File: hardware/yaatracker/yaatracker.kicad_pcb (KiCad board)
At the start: 2 copper layers, 62 parts, among them J1 USB_MINI, P1 TP_URX, P10 BATT, P11 MBUTTON2, P12 ICSP_CONN5, P13 I2C_SCREEN, P14 R_VCC, P15 GPS_DE9, P16 RADIO_DE9, P2 GPIO10_GND_JUMPER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

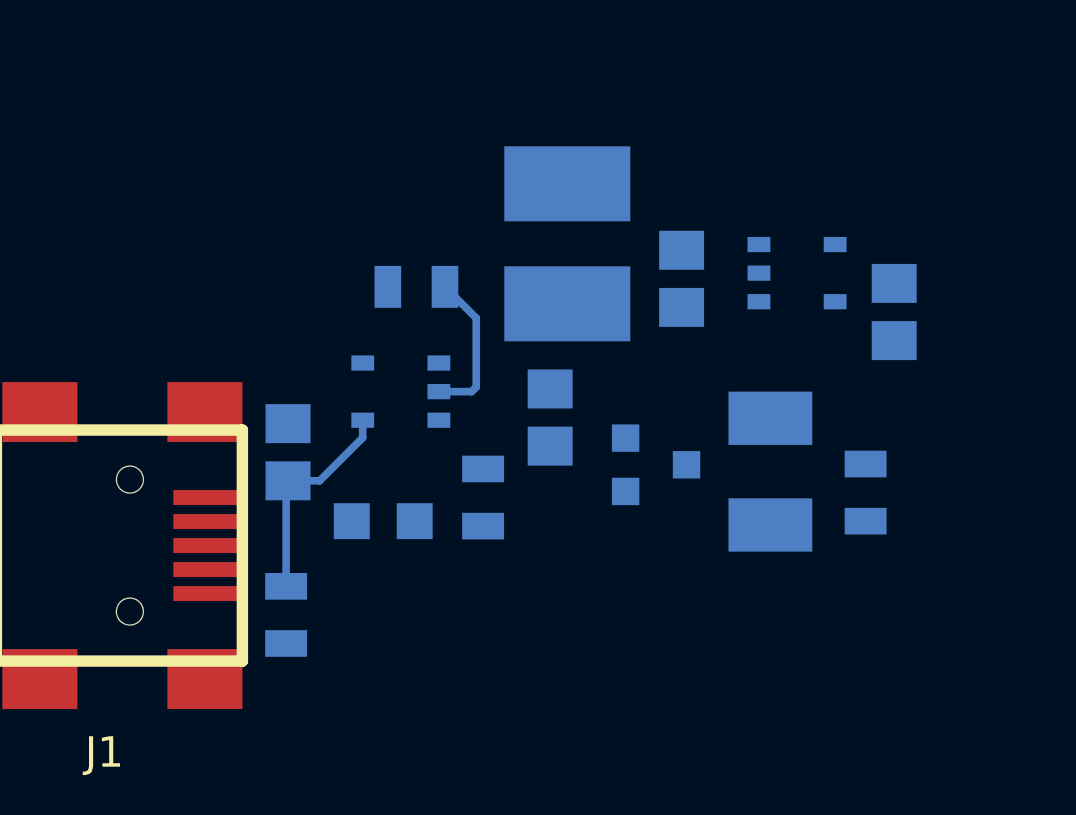
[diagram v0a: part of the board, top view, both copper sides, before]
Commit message: PCB layout power circuit finished
Layout of the power circuit is now finished
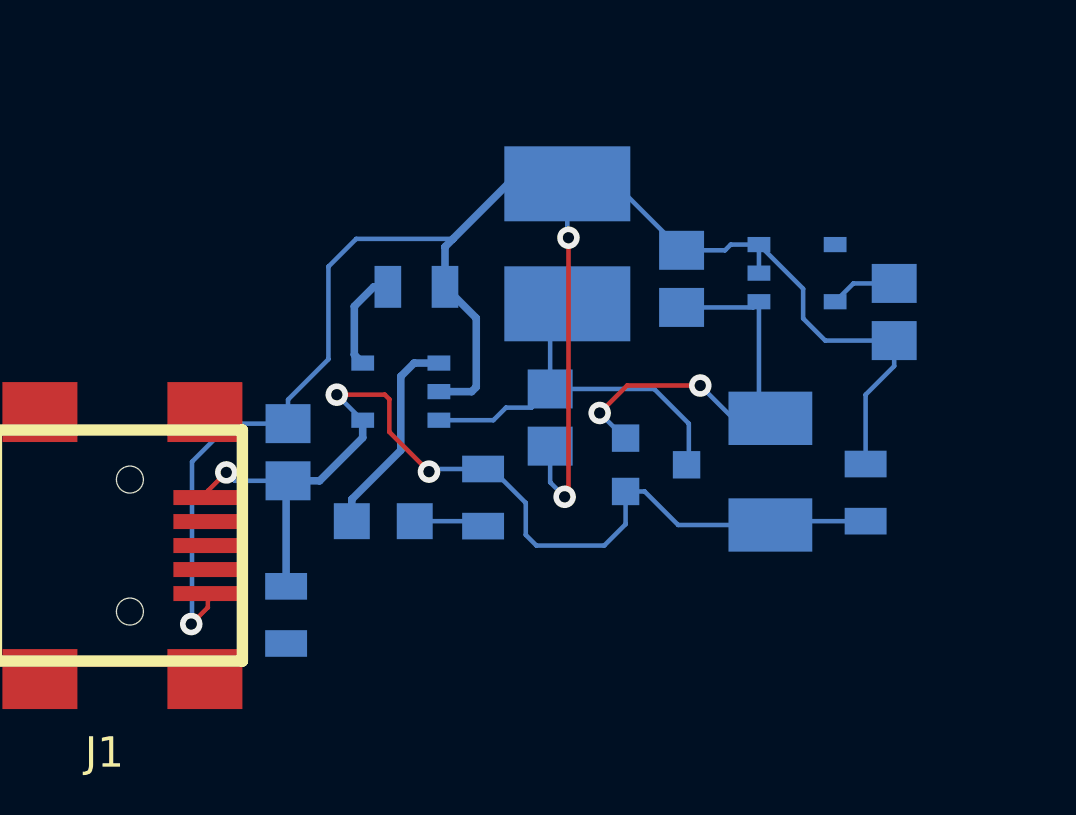
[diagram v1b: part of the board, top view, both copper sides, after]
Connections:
- R18 pad 1: N-0000026 (its old number) -> GND
- U4 pad 2: N-0000026 (its old number) -> GND
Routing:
- net GND: track 0.00 -> 63.7 mm, vias 0 -> 3
- net N-0000035: track 7.21 -> 34.6 mm, vias 0 -> 3
- net N-0000025: track 0.00 -> 14.4 mm, vias 0 -> 2
- net N-0000027: track 0.00 -> 13.7 mm
- net N-0000036: track 0.00 -> 6.96 mm
- net N-0000026 (its old number): track 5.08 -> 0.00 mm
- net N-0000024: track 0.00 -> 3.39 mm
- net N-0000037: track 0.00 -> 2.35 mm
- net +3.3V: track 0.00 -> 2.22 mm
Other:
- net class Default: clearance 0.254 -> 0.1524; trace_width 0.254 -> 0.1524; via_dia 0.889 -> 0.75; via_drill 0.635 -> 0.5
- net class power added: clearance 0.1524, trace_width 0.23, via_dia 0.75, via_drill 0.5
- rule trace_clearance: 0.254 -> 0.1524
- rule trace_min: 0.254 -> 0.1524
- rule via_min_drill: 0.508 -> 0.4
- rule via_min_size: 0.889 -> 0.75

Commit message: More PCB layout
ICSP connector done, as well as screen/I2C connector, and a few buttons.
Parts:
- moved P12 222.6 mm to (113.7, 120.4), turned to 180 degrees
- moved R17 220.5 mm to (122.5, 124.0)
- moved R14 216.5 mm to (123.9, 127.0), turned to 90 degrees
- moved R13 214.3 mm to (122.2, 131.1), turned to 90 degrees
- moved R15 195.0 mm to (136.6, 123.3)
- moved C10 192.1 mm to (113.7, 140.0), turned to 180 degrees
- moved P13 122.0 mm to (133.0, 120.0)
- moved R16 100.2 mm to (121.5, 127.3), turned to 270 degrees
- moved R12 88.3 mm to (130.5, 123.1), turned to 180 degrees
- moved U3 39.7 mm to (122.5, 139.4)
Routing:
- net N-000001: track 0.00 -> 49.9 mm
- net +3.3V: track 2.22 -> 39.1 mm, vias 0 -> 2
- net GND: track 63.7 -> 99.3 mm, vias 3 -> 4
- net N-0000020: track 0.00 -> 29.4 mm
- net N-0000021: track 0.00 -> 24.0 mm
- net N-0000044: track 0.00 -> 21.5 mm, vias 0 -> 2
- net N-0000043: track 0.00 -> 17.1 mm
- net N-0000019: track 0.00 -> 9.77 mm
- net N-000007: track 0.00 -> 6.93 mm
- net N-000008: track 0.00 -> 2.82 mm
- net N-0000011: track 0.00 -> 2.27 mm
- net N-000009: track 0.00 -> 2.24 mm
- net N-0000035: track 34.6 -> 33.3 mm

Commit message: Some more PCB layout
Some more PCB layout. Forgot to connect two grounds together.
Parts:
- C8: moved to B.Cu
- moved R5 205.8 mm to (140.8, 141.3), turned to 180 degrees
- moved R11 203.5 mm to (138.8, 138.4), turned to 270 degrees
- moved C4 188.0 mm to (141.7, 138.2), turned to 270 degrees
- moved C8 169.3 mm to (130.5, 138.0), turned to 90 degrees
- moved U2 133.5 mm to (133.5, 138.0)
- moved P15 102.1 mm to (142.4, 124.5), turned to 270 degrees
- moved P8 96.4 mm to (136.8, 132.0)
- moved R8 81.0 mm to (136.7, 141.1), turned to 180 degrees
- moved P16 58.2 mm to (209.8, 131.2), turned to 270 degrees
- moved RV2 55.8 mm to (162.4, 131.3)
- moved P4 49.7 mm to (157.3, 153.5)
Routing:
- net (no net): track 0.00 -> 28.8 mm
- net +3.3V: track 39.1 -> 64.5 mm, vias 2 -> 4
- net /UART_RX: track 0.00 -> 22.0 mm
- net N-0000038: track 0.00 -> 18.1 mm
- net N-000003: track 0.00 -> 7.39 mm, vias 0 -> 2
- net GND: track 99.3 -> 106.6 mm
- net N-0000042: track 0.00 -> 6.39 mm, vias 0 -> 1
- net N-000004: track 0.00 -> 6.36 mm
- net N-000005: track 0.00 -> 4.46 mm
- net N-000006: track 0.00 -> 2.15 mm

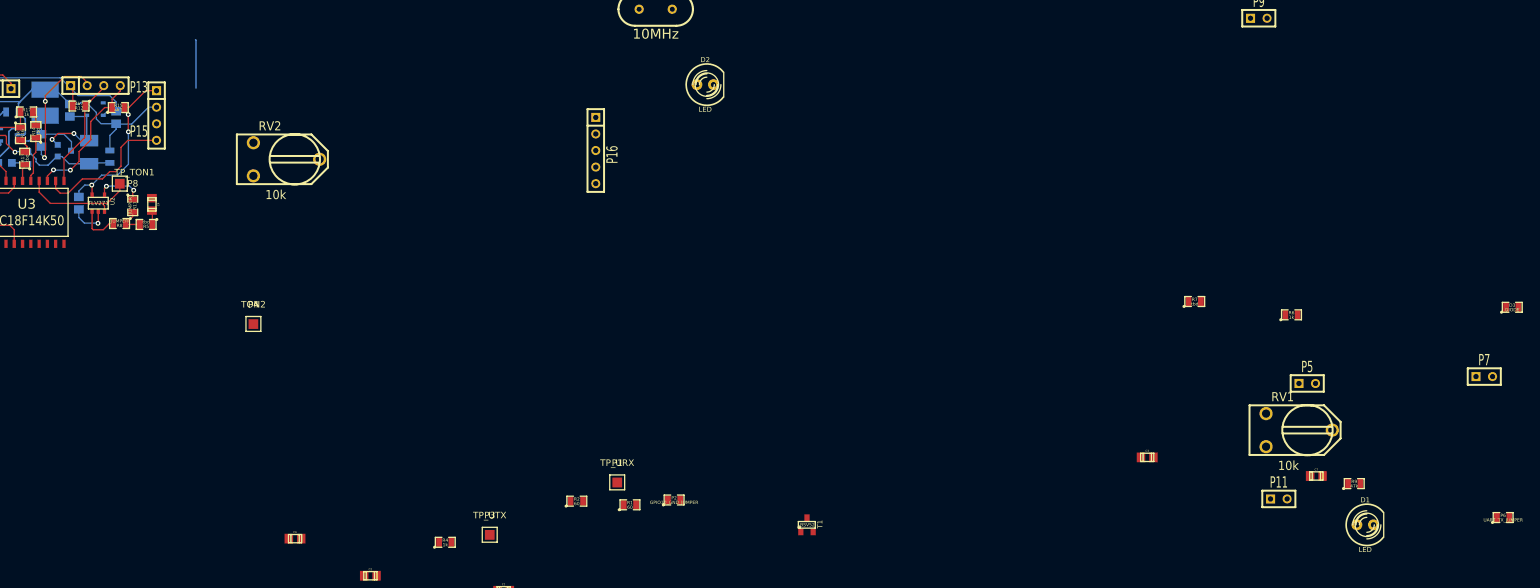
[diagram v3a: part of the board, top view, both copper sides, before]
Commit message: Traces to GPS conn, audio out
Routed traces to GPS uart connector, and audio out done to pot.
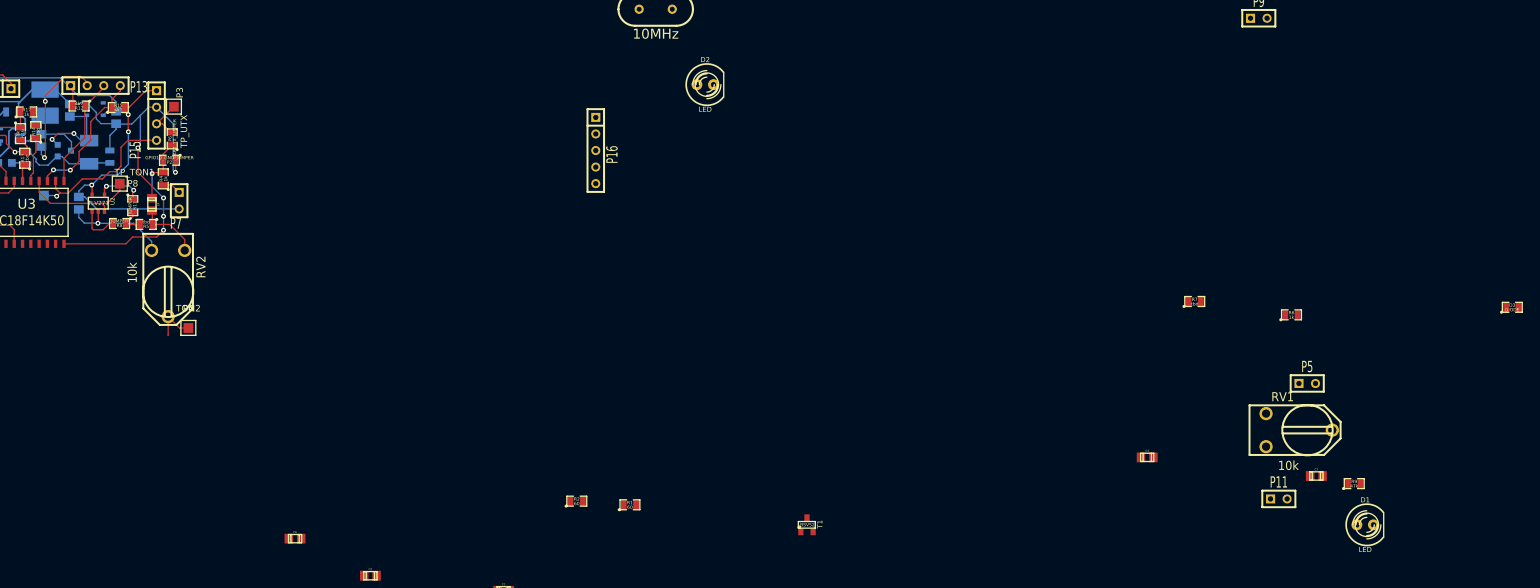
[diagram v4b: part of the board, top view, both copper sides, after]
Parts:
- P1: moved to B.Cu
- moved P6 212.3 mm to (144.8, 128.1), turned to 90 degrees
- moved P7 202.1 mm to (145.9, 137.6), turned to 270 degrees
- moved P1 95.8 mm to (125.1, 139.8)
- moved P2 93.3 mm to (144.4, 131.4), turned to 180 degrees
- moved P3 81.6 mm to (145.1, 120.2)
- moved R4 70.6 mm to (143.4, 134.3), turned to 90 degrees
- moved RV2 26.3 mm to (144.2, 150.3), turned to 270 degrees
- moved P4 10.0 mm to (147.3, 154.2)
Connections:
- C4 pad 2: N-0000042 -> GND
- C7 pad 2: N-0000042 -> GND
- C8 pad 2: N-0000042 -> GND
- R6 pad 1: N-0000042 -> GND
- RV2 pad 3: N-0000042 -> GND
- T1 pad 2: N-0000042 -> GND
- U2 pad 2: N-0000042 -> GND
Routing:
- net GND: track 106.6 -> 150.6 mm, vias 4 -> 7
- net N-0000018: track 0.00 -> 32.1 mm, vias 0 -> 4
- net +3.3V: track 64.5 -> 80.6 mm
- net N-000001: track 2.15 -> 9.75 mm
- net (no net): track 28.8 -> 21.3 mm
- net /UART_TX: track 0.00 -> 6.71 mm
- net /AUDIO_OUT: track 0.00 -> 6.68 mm
- net N-0000042: track 6.39 -> 0.00 mm, vias 1 -> 0
- net N-000007: track 0.00 -> 2.91 mm
- net /UART_RX: track 22.0 -> 24.7 mm, vias 0 -> 1

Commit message: PCB layout almost finished
Lacking LEDs, and a few buttons to be routed.
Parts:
- moved D3 231.9 mm to (120.0, 180.5)
- moved P11 210.2 mm to (108.4, 142.9)
- moved P5 208.4 mm to (110.8, 175.3)
- moved P9 203.1 mm to (111.9, 147.1)
- moved R9 201.7 mm to (126.1, 155.3), turned to 270 degrees
- moved C7 194.3 mm to (127.1, 159.2), turned to 180 degrees
- moved RV1 186.6 mm to (132.2, 153.7), turned to 270 degrees
- moved C3 157.6 mm to (137.9, 158.8), turned to 180 degrees
- moved R3 122.5 mm to (119.6, 176.7)
- moved T1 117.6 mm to (127.3, 162.3), turned to 270 degrees
- moved X1 110.9 mm to (116.9, 151.5), turned to 180 degrees
- moved C1 97.9 mm to (108.4, 153.2), turned to 180 degrees
- moved C2 80.3 mm to (108.4, 150.6), turned to 180 degrees
- moved P16 75.3 mm to (142.0, 164.1), turned to 0 degrees
- moved C6 68.1 mm to (113.9, 142.9), turned to 180 degrees
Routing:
- net GND: track 150.6 -> 223.5 mm, vias 7 -> 11
- net +3.3V: track 80.6 -> 131.7 mm, vias 4 -> 5
- net /R_VOUT: track 0.00 -> 47.7 mm, vias 0 -> 2
- net N-0000011: track 2.27 -> 39.7 mm, vias 0 -> 2
- net N-0000010: track 2.24 -> 36.3 mm, vias 0 -> 1
- net N-0000025: track 0.00 -> 21.5 mm
- net N-0000028: track 0.00 -> 18.2 mm
- net N-0000027: track 0.00 -> 14.2 mm
- net N-0000040: track 0.00 -> 10.3 mm
- net /PTT: track 0.00 -> 8.06 mm
- net /AUDIO_OUT: track 6.68 -> 13.9 mm
- net /AUDIO_IN: track 0.00 -> 5.48 mm
- net N-0000041: track 0.00 -> 5.13 mm
- net N-0000033: track 33.3 -> 32.4 mm

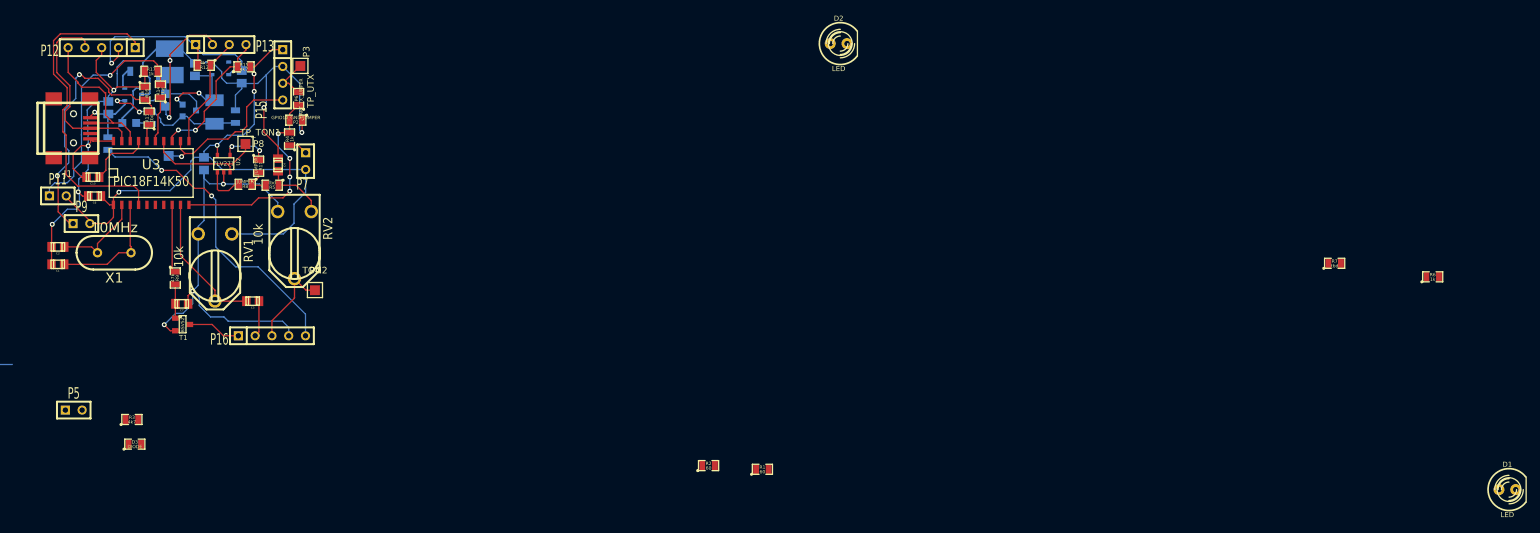
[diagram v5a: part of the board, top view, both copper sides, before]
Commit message: PCB layout routing done
PCB layout traces routing done, but need to add a button connected to pin 7 (pull down
and current-limiting resistor already exist in design).
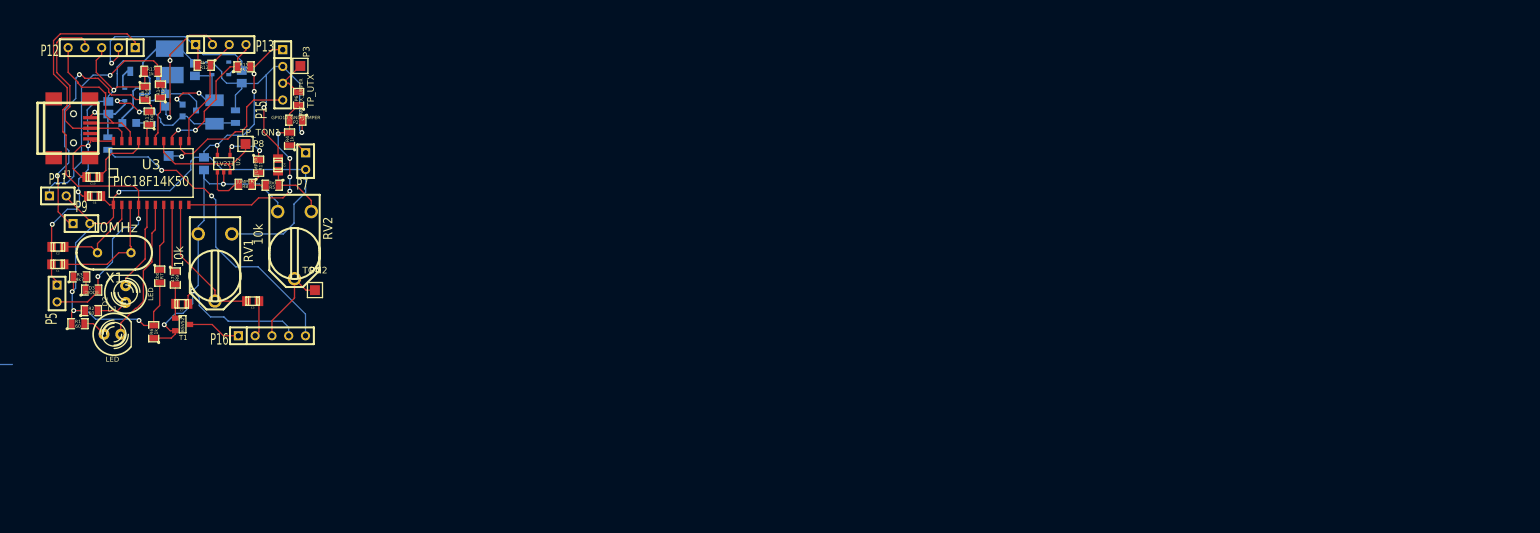
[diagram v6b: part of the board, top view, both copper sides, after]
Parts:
- moved D1 212.5 mm to (116.6, 163.8)
- moved R6 193.9 mm to (122.9, 163.4), turned to 90 degrees
- moved R7 177.9 mm to (123.8, 155.0), turned to 270 degrees
- moved D2 114.4 mm to (118.6, 157.7), turned to 90 degrees
- moved R1 106.0 mm to (111.4, 162.2)
- moved R2 96.4 mm to (113.4, 160.2)
- moved D3 24.2 mm to (113.5, 157.1)
- moved R3 23.0 mm to (111.7, 155.1)
- moved P5 17.8 mm to (108.2, 157.7), turned to 270 degrees
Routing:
- net +3.3V: track 131.7 -> 172.1 mm, vias 5 -> 8
- net N-000002: track 49.9 -> 73.4 mm, vias 0 -> 2
- net N-0000016: track 0.00 -> 21.9 mm
- net N-0000017: track 0.00 -> 13.6 mm
- net N-0000013: track 0.00 -> 10.1 mm
- net GND: track 223.5 -> 231.0 mm
- net N-0000015: track 0.00 -> 4.75 mm
- net N-0000014: track 0.00 -> 3.66 mm
- net N-000003: track 0.00 -> 2.03 mm

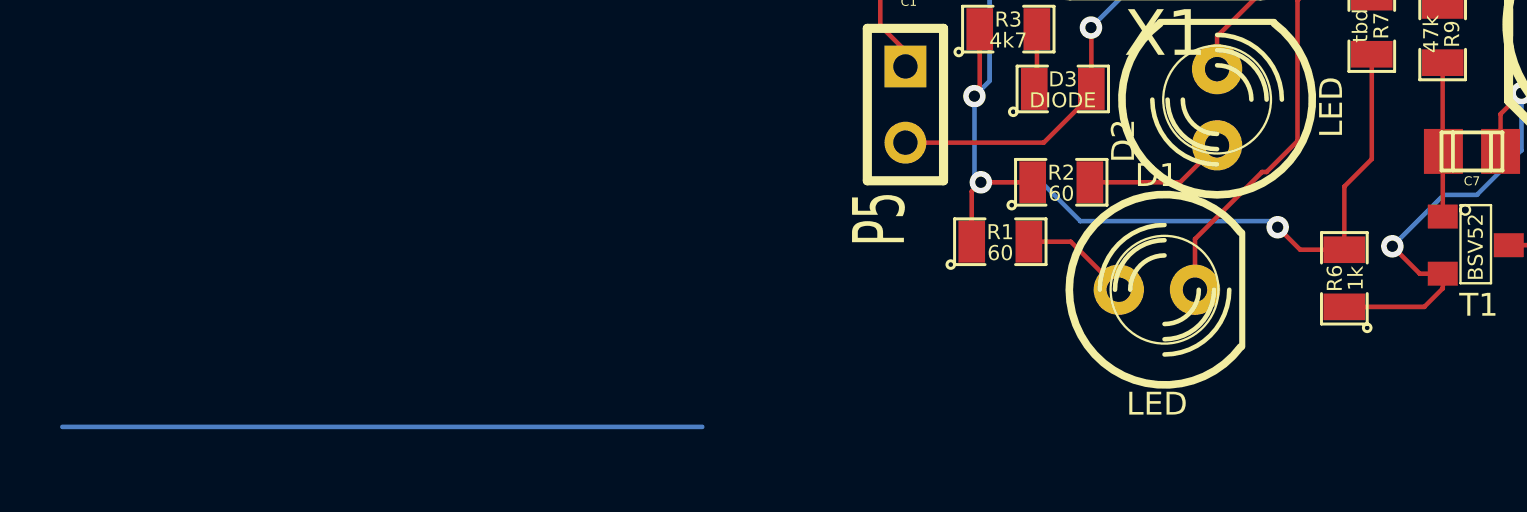
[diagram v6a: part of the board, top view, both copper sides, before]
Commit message: PCB layout last switch
Added and routed another switch successfully.
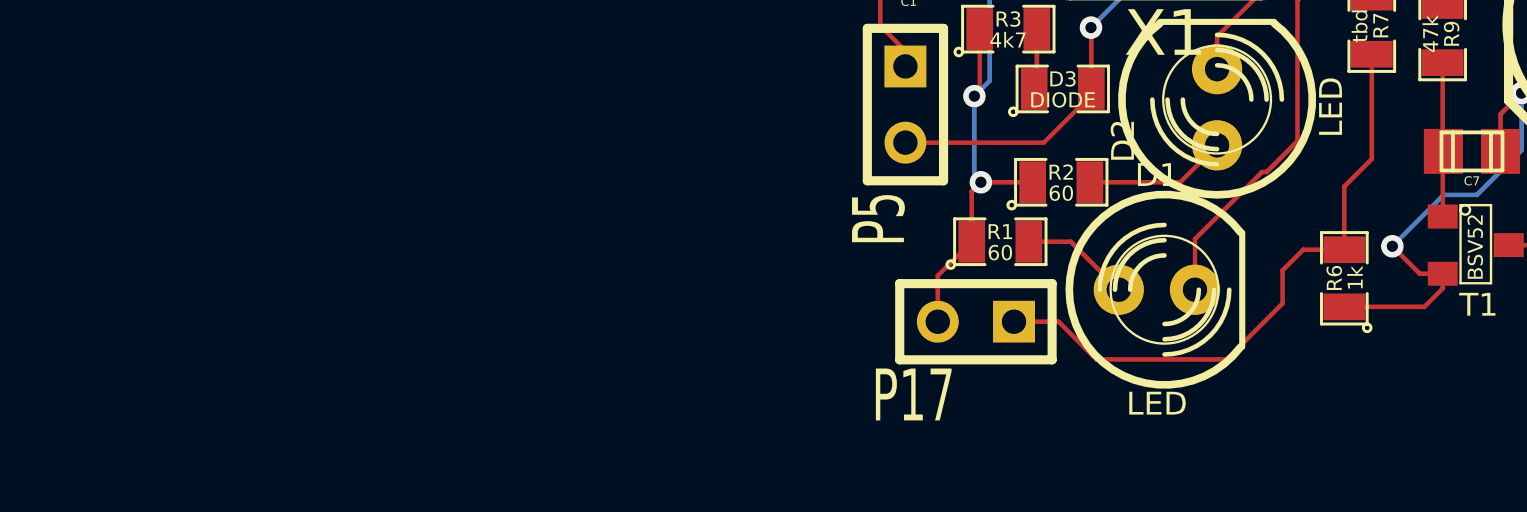
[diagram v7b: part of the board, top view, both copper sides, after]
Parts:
- added P17: SW5, SIL-2, F.Cu at (110.6, 164.9)
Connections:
- R6 pad 2: +3.3V -> N-0000020
- R7 pad 2: +3.3V -> N-0000020
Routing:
- net (no net): track 21.3 -> 0.00 mm
- net N-0000020: track 0.00 -> 20.6 mm
- net +3.3V: track 172.1 -> 155.3 mm, vias 8 -> 7
